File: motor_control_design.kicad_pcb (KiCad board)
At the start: 2 copper layers, 57.1 x 57.2 mm, 90 parts, among them J1 TYPE-C-31-M-12, J10 5V, J2 SWD, J3 VBAT, J4 GND, J5 FC_M/P, J6 Conn_01x06, J7 Conn_01x04_Pin, J9 GND, Q1 RF1S9540SM, Q10 2N7002, Q11 2N7002, Q12 2N7002, Q13 2N7002, Q14 RF1S9540SM, Q15 IRLZ44NS, Q16 2N7002, Q2 RF1S9540SM, Q3 IRLZ44NS, Q4 2N7002, Q5 2N7002, Q6 RF1S9540SM, Q7 IRLZ44NS, Q8 2N7002, Q9 IRLZ44NS, U1 STM32F401CCU6, U2 LT1962-3.3, U4 TPS563200, Y1 16MHz

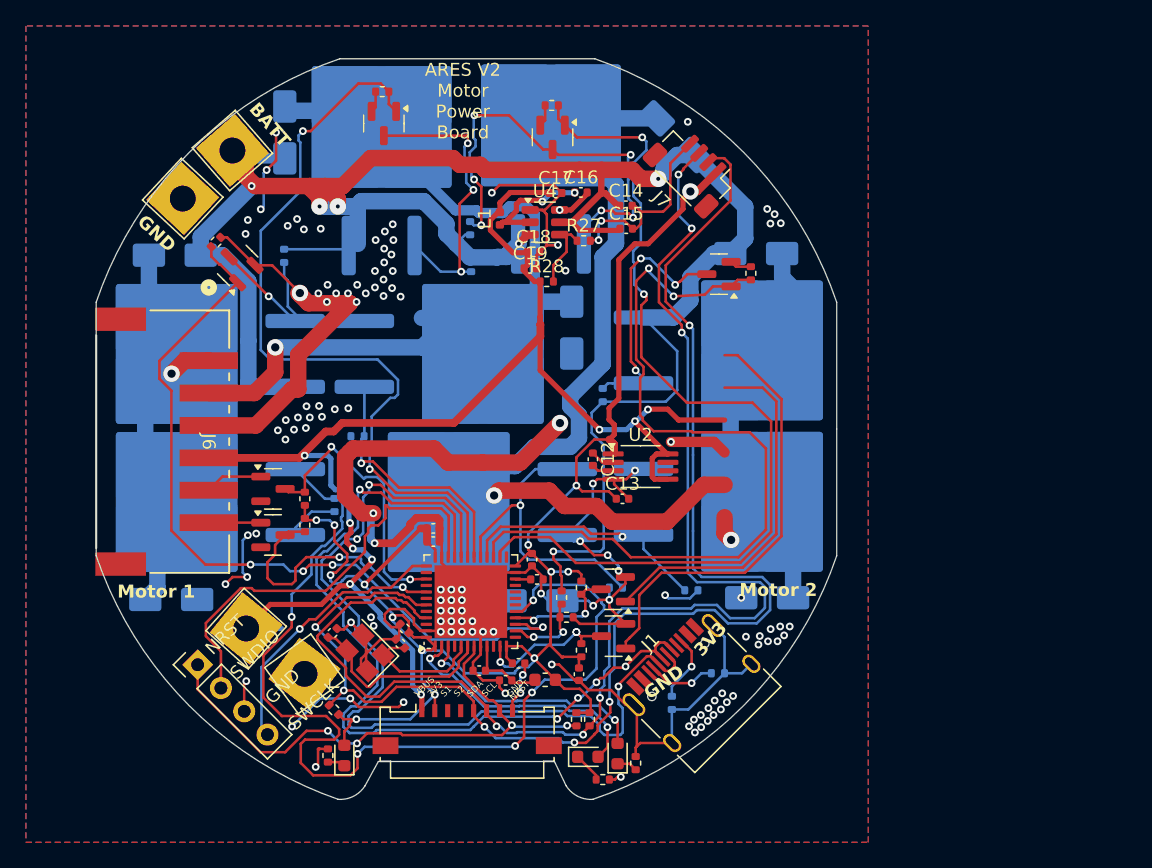
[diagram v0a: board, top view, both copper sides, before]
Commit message: Cleaned up traces after shifting last night
Cleaned up traces after shifting last night
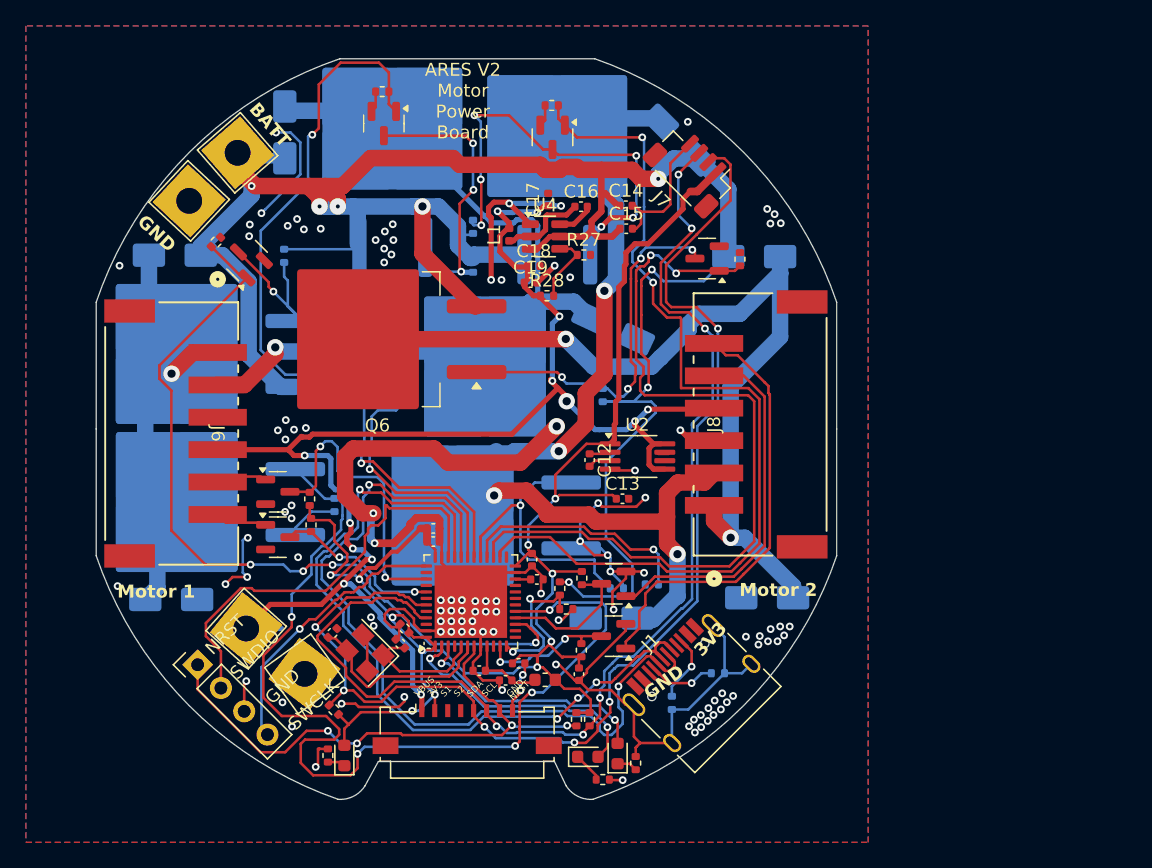
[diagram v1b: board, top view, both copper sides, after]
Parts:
- removed Q7: IRLZ44NS, Package_TO_SOT_SMD:TO-263-2
- added J8: Conn_01x06, CustomARES:CONN_S6B-XH-SM4-TB_JST, F.Cu at (171.7, 88.8)
- J6: footprint Custom:CONN_S6B-XH-SM4-TB_JST -> CustomARES:CONN_S6B-XH-SM4-TB_JST
- Q6: moved to F.Cu
- moved Q6 28.2 mm to (142.1, 82.2), turned to 180 degrees
- moved D12 5.95 mm to (160.2, 103.7), turned to 180 degrees
- moved D6 3.20 mm to (160.3, 81.3), turned to -25 degrees
- moved R19 3.08 mm to (163.3, 101.1), turned to 180 degrees
- moved Q5 1.51 mm to (167.6, 76.0)
- moved L1 1.43 mm to (152.3, 74.1)
- moved R17 1.37 mm to (170.1, 76.0)
- moved C16 1.10 mm to (157.8, 71.9)
- moved C18 1.10 mm to (154.2, 76.5)
- moved C19 1.10 mm to (153.9, 77.8)
- moved R27 1.10 mm to (158.1, 75.7)
- moved R28 1.10 mm to (155.2, 78.8)
- moved U4 1.10 mm to (155.1, 74.2)
- moved Q15 1.07 mm to (149.4, 95.8)
- moved Q3 0.98 mm to (148.9, 84.3)
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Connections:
- U1 pad 12: +3.3V -> /VBatt_sense
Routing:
- net /M2A: track 19.5 -> 70.3 mm, vias 1 -> 2
- net GND: track 248.4 -> 199.6 mm, vias 126 -> 111
- net +BATT: track 168.1 -> 182.8 mm, vias 6 -> 8
- net /SCL: track 102.3 -> 90.3 mm
- net /SDA: track 107.8 -> 96.3 mm
- net Net-(Q5-D): track 20.1 -> 29.1 mm, vias 3 -> 4
- net /E1B: track 21.0 -> 13.0 mm
- net /USB_D+: track 65.5 -> 59.3 mm, vias 5 -> 4
- net /USB_D-: track 69.2 -> 63.0 mm, vias 3 -> 2
- net /VBatt_sense: track 6.37 -> 11.0 mm
- net /M1Q3: track 60.4 -> 64.6 mm
- net /M1Q2: track 77.4 -> 74.6 mm
- net +5V: track 114.6 -> 111.9 mm, vias 9 -> 13
- net /M2B: track 67.5 -> 70.2 mm, vias 1 -> 4
- net Net-(U4-SW): track 9.32 -> 6.76 mm, vias 2 -> 0
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
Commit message: ADR2
Put the 8th mosfet back, fixed all of ethans criteia
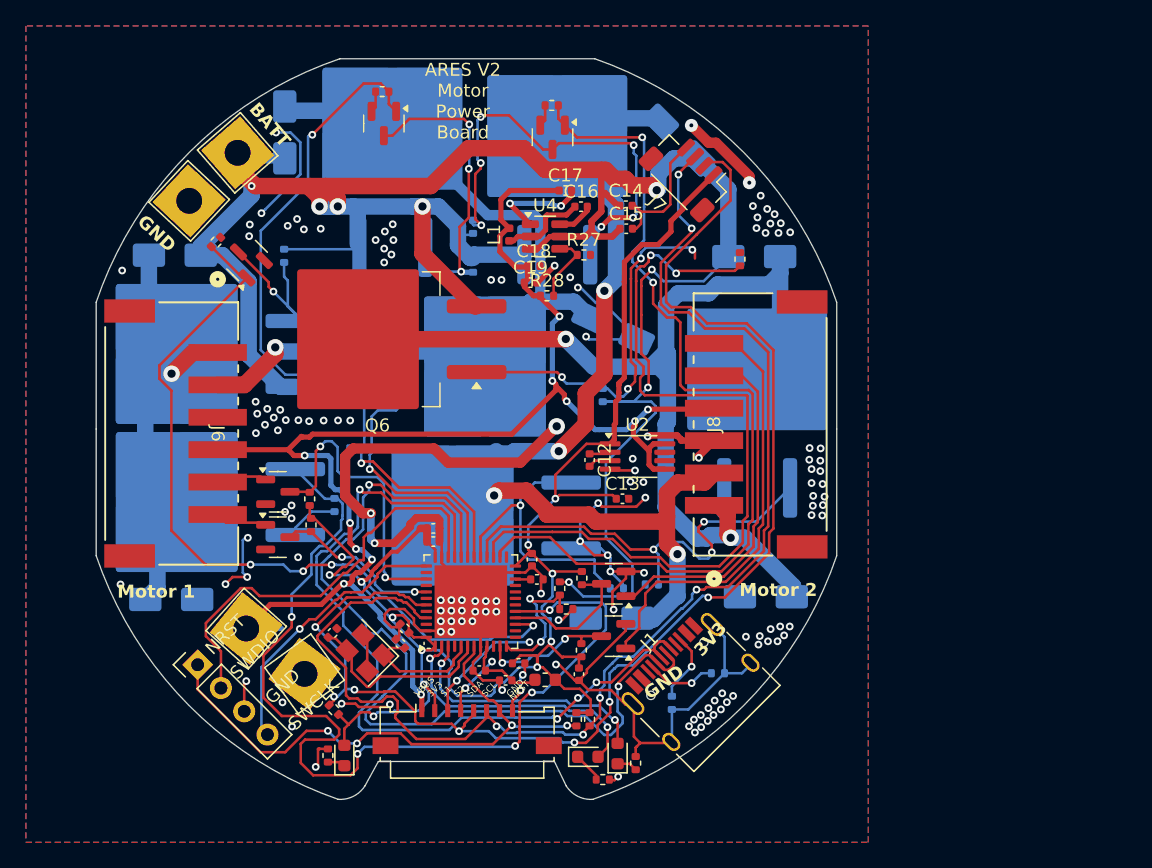
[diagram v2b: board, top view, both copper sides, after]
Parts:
- removed Q5: 2N7002, Package_TO_SOT_SMD:SOT-23
- added Q7: IRLZ44NS, Package_TO_SOT_SMD:TO-263-2, B.Cu at (171.4, 86.0)
- moved C17 1.50 mm to (156.6, 70.7), turned to 0 degrees
- moved J7 0.43 mm to (166.1, 69.4)
- moved D9 0.12 mm to (172.1, 102.0)
- moved J1 0.11 mm to (167.1, 109.5)
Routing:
- net /M2Q2: track 18.2 -> 34.4 mm, vias 1 -> 3
- net GND: track 199.6 -> 212.2 mm, vias 111 -> 142
- net /M2A: track 70.3 -> 80.7 mm
- net /S1: track 0.00 -> 9.45 mm, vias 0 -> 2
- net /SCL: track 90.3 -> 99.7 mm
- net /SDA: track 96.3 -> 103.4 mm, vias 6 -> 7
- net /USB_D-: track 63.0 -> 68.1 mm
- net /S2: track 0.00 -> 4.79 mm, vias 0 -> 2
- net /M1Q3: track 64.6 -> 60.4 mm
- net /USB_D+: track 59.3 -> 63.4 mm
- net +3.3V: track 130.6 -> 134.2 mm
- net +5V: track 111.9 -> 113.5 mm, vias 13 -> 11
- net +BATT: track 182.8 -> 184.4 mm
- net Net-(Q1-G): track 22.1 -> 23.5 mm
- net /M2Q3: track 70.6 -> 69.2 mm
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
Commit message: layout changes started, ov regulator wip
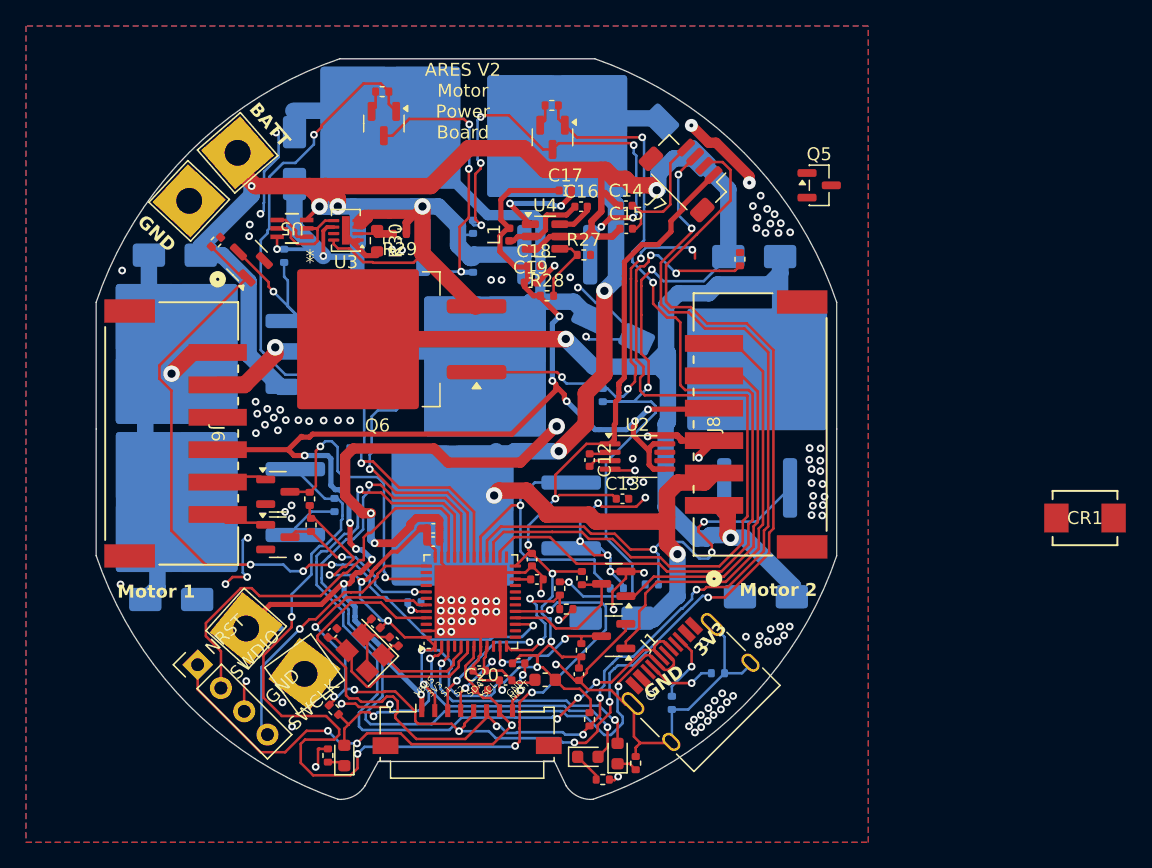
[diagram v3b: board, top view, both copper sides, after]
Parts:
- added C20: 100nF, Capacitor_SMD:C_0402_1005Metric, F.Cu at (150.2, 109.2)
- added CR1: SMBJ15A, CustomARES:DO-214AASMB_J-BEND_LTF, F.Cu at (196.7, 96.0)
- added Q5: 2N7002, Package_TO_SOT_SMD:SOT-23, F.Cu at (176.2, 70.3)
- added R29: 15k, Resistor_SMD:R_0402_1005Metric, F.Cu at (143.8, 74.0)
- added R30: 470, Resistor_SMD:R_0603_1608Metric, F.Cu at (142.1, 74.6)
- added U3: LTC4365DDB, Package_DFN_QFN:DFN-8-1EP_2x3mm_P0.5mm_EP0.61x2.2mm, F.Cu at (139.7, 73.8)
- added U5: SSM6N7002KFU_LF, CustomARES:SOT-363 US6_TOS-M, F.Cu at (135.5, 73.6)
- R3: moved to B.Cu
- moved R3 15.4 mm to (145.0, 102.5), turned to 0 degrees
- moved C4 2.26 mm to (142.0, 104.1)
- moved D7 2.12 mm to (135.7, 68.2)
- moved C2 0.52 mm to (143.4, 105.5)
- moved Q1 0.17 mm to (143.1, 67.3)
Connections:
- D10 pad 1: +BATT -> VMOTOR
- D4 pad 1: +BATT -> VMOTOR
- D7 pad 1: +BATT -> VMOTOR
- D8 pad 1: +BATT -> VMOTOR
- Q1 pad 3: +BATT -> VMOTOR
- Q14 pad 3: +BATT -> VMOTOR
- Q2 pad 3: +BATT -> VMOTOR
- Q6 pad 3: +BATT -> VMOTOR
- R13 pad 2: +BATT -> VMOTOR
- R14 pad 2: +BATT -> VMOTOR
- R18 pad 2: +BATT -> VMOTOR
- R20 pad 2: +BATT -> VMOTOR
- R3 pad 1: +3.3V -> Net-(U1-BOOT0)
- R3 pad 2: /NRST -> GND
- U1 pad 44: unconnected-(U1-BOOT0-Pad44) -> Net-(U1-BOOT0)
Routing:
- net VMOTOR: track 0.00 -> 16.9 mm, vias 0 -> 2
- net +BATT: track 184.4 -> 193.7 mm
- net Net-(U3-GATE): track 0.00 -> 8.01 mm
- net /NRST: track 43.9 -> 39.0 mm, vias 4 -> 3
- net +3.3V: track 134.2 -> 130.5 mm
- net /SRC: track 0.00 -> 3.05 mm
- net Net-(U3-OV): track 0.00 -> 2.74 mm
- net /USB_D-: track 68.1 -> 65.7 mm
- net GND: track 212.2 -> 210.1 mm, vias 142 -> 133
- net Net-(U1-BOOT0): track 0.00 -> 1.92 mm, vias 0 -> 1

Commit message: layout completed with ov, tvs; only board edge and footprint drc err
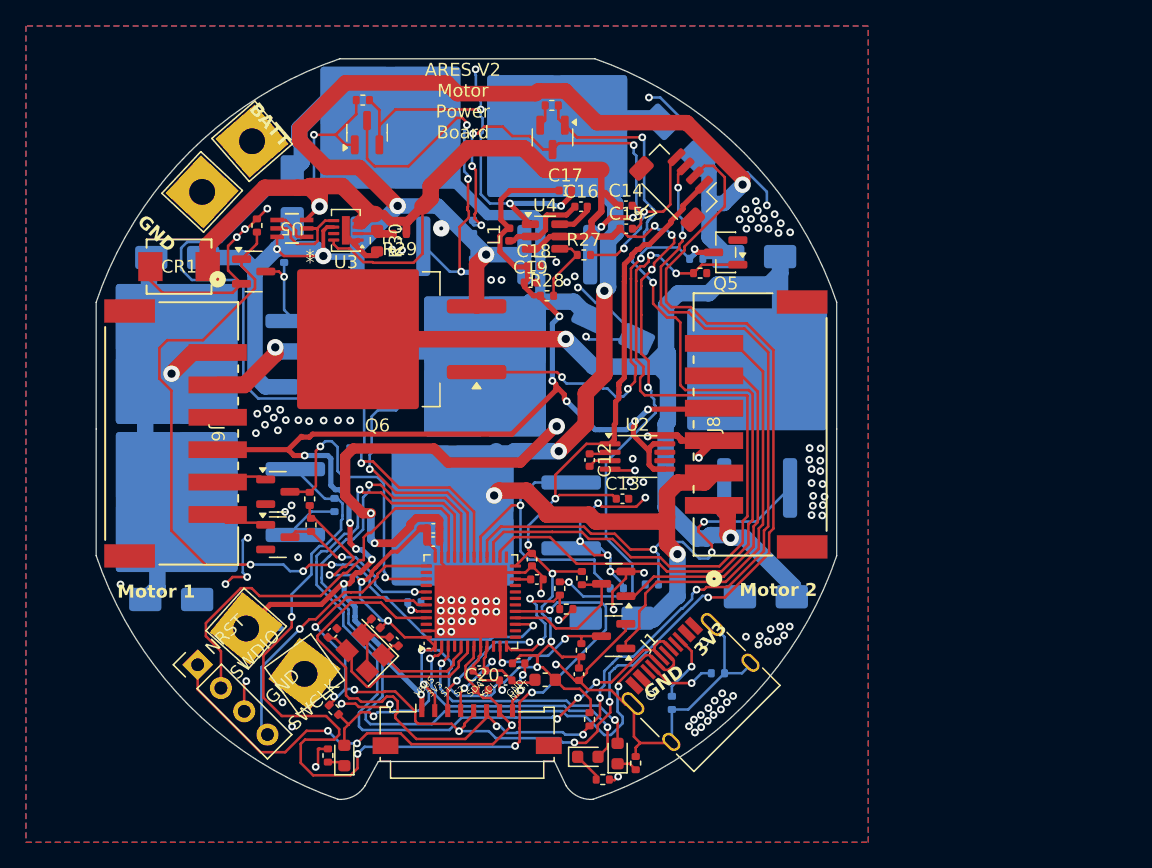
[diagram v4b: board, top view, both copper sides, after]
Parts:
- moved CR1 72.6 mm to (126.8, 76.6)
- moved R18 12.7 mm to (166.7, 76.0), turned to 0 degrees
- moved Q5 8.88 mm to (169.0, 75.5), turned to 180 degrees
- moved R4 3.41 mm to (132.8, 73.4), turned to 90 degrees
- moved R17 3.26 mm to (167.0, 77.1), turned to 0 degrees
- moved D7 3.03 mm to (135.6, 71.2)
- moved R6 1.63 mm to (141.0, 63.7), turned to 0 degrees
- moved Q4 1.48 mm to (141.3, 66.2), turned to 90 degrees
- moved J3 1.43 mm to (132.4, 66.9)
- moved J4 1.21 mm to (128.6, 70.8)
- moved J7 1.04 mm to (165.3, 70.1)
- moved Q13 0.98 mm to (132.6, 77.0), turned to 0 degrees
- moved D4 0.26 mm to (126.7, 75.9)
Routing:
- net VMOTOR: track 16.9 -> 124.6 mm, vias 2 -> 6
- net +BATT: track 193.7 -> 117.8 mm, vias 8 -> 6
- net GND: track 210.1 -> 252.0 mm, vias 133 -> 137
- net /M1Q3: track 60.8 -> 70.5 mm
- net Net-(Q1-G): track 23.5 -> 29.2 mm
- net Net-(Q13-D): track 11.9 -> 6.46 mm
- net /M1B: track 54.7 -> 58.4 mm
- net /M1Q1: track 60.6 -> 63.1 mm
- net Net-(Q5-D): track 29.1 -> 30.9 mm
- net /SCL: track 99.4 -> 97.9 mm
- net +3.3V: track 130.5 -> 129.1 mm
- net Net-(Q14-G): track 35.5 -> 34.4 mm
- net /M2Q3: track 69.2 -> 69.9 mm

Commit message: clean up
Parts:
- moved C12 0.07 mm to (158.4, 91.5)
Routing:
- net +BATT: track 117.8 -> 121.8 mm

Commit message: nothing
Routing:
- net +BATT: track 121.8 -> 120.6 mm
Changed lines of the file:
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@@
+	)
+	(segment
+		(start 136.906 70.485)
+		(end 137.656858 71.235858)
+		(width 1.27)
+		(layer "F.Cu")
+		(net 7)
 	)
 	(segment
@@
 		(end 156.899483 100.915914)
 		(width 0.2)
-		(layer "F.Cu")
-		(net 7)
-	)
-	(segment
-		(start 133.44 67.89)
-		(end 132.45 66.9)
-		(width 1.27)
 		(layer "F.Cu")
 		(net 7)
@@
 	)
 	(segment
+		(start 133.44 67.89)
+		(end 133.44 70.485)
+		(width 1.27)
+		(layer "F.Cu")
+		(net 7)
+	)
+	(segment
 		(start 146.235453 70.358)
 		(end 149.154453 67.439)
@@
 	)
 	(segment
-		(start 135.96 70.485)
-		(end 133.44 70.485)
-		(width 1.27)
-		(layer "F.Cu")
-		(net 7)
-	)
-	(segment
 		(start 141.425 72.85)
 		(end 140.926 73.349)
@@
 	)
 	(segment
-		(start 136.906 70.485)
-		(end 135.96 70.485)
-		(width 1.27)
-		(layer "F.Cu")
-		(net 7)
-	)
-	(segment
 		(start 137.656858 71.930669)
 		(end 137.656858 71.235858)
@@
 		(end 163.301436 76.801436)
 		(width 0.2)
-		(layer "F.Cu")
-		(net 7)
-	)
-	(segment
-		(start 136.906 70.358)
-		(end 136.906 70.485)
-		(width 1.27)
-		(layer "F.Cu")
-		(net 7)
-	)
-	(segment
-		(start 133.44 70.485)
-		(end 133.44 67.89)
-		(width 1.27)
 		(layer "F.Cu")
 		(net 7)
@@
 	)
 	(segment
+		(start 133.44 70.485)
+		(end 136.906 70.485)
+		(width 1.27)
+		(layer "F.Cu")
+		(net 7)
+	)
+	(segment
 		(start 141.425 72.539)
 		(end 141.425 72.85)
@@
 	)
 	(segment
+		(start 132.45 66.9)
+		(end 133.44 67.89)
+		(width 1.27)
+		(layer "F.Cu")
+		(net 7)
+	)
+	(segment
 		(start 141.03026 76.226)
 		(end 141.751 76.226)
@@
 		(start 149.154453 67.439)
 		(end 153.404927 67.439)
-		(width 1.27)
-		(layer "F.Cu")
-		(net 7)
-	)
-	(segment
-		(start 136.906 70.485)
-		(end 137.619262 71.198262)
 		(width 1.27)
 		(layer "F.Cu")
@@
 	)
 	(segment
+		(start 137.656858 71.235858)
+		(end 140.721858 71.235858)
+		(width 1.27)
+		(layer "F.Cu")
+		(net 7)
+	)
+	(segment
 		(start 162.83 85.73)
 		(end 162.83 83.63)
@@
 	)
 	(segment
-		(start 138.0998 70.358)
-		(end 139.408 70.358)
+		(start 140.721858 71.235858)
+		(end 142 72.514)
 		(width 1.27)
 		(layer "F.Cu")
@@
 	)
 	(segment
-		(start 141.564 72.514)
-		(end 141.95 72.514)
-		(width 1.27)
-		(layer "F.Cu")
-		(net 7)
-	)
-	(segment
 		(start 153.404927 67.439)
 		(end 155.072428 69.106501)
@@
 	)
 	(segment
-		(start 136.906 70.358)
-		(end 138.0998 70.358)
-		(width 1.27)
-		(layer "F.Cu")
-		(net 7)
-	)
-	(segment
 		(start 161.47845 74.261)
 		(end 161.224 74.00655)
@@
 		(layer "F.Cu")
 		(net 7)
-	)
-	(segment
-		(start 139.408 70.358)
-		(end 141.564 72.514)
-		(width 1.27)
-		(layer "F.Cu")
-		(net 7)
